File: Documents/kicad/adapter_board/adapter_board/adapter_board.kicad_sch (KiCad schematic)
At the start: 4 parts, among them J1 NPTC081KFXC-RC, J2 NPPN101BFLC-RC, J3 NPPN101BFLC-RC, J4 NPTC081KFXC-RC

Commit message: adapter board changes
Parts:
- J1: value NPTC081KFXC-RC -> ESP Cam Left
- J2: value NPPN101BFLC-RC -> Crazyflie Left
- J3: value NPPN101BFLC-RC -> Crazyflie Right
- J4: value NPTC081KFXC-RC -> ESP Cam Right
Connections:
- net VCOM: now reaches J3.9
- net GND: now reaches J1.7
- net GND: now also J2.10
- net 3.3 V Connect renamed 3v3
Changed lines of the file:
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@@
 	(generator_version "8.0")
 	(paper "A4")
+	(wire
+		(pts
+			(xy 64.77 127) (xy 72.39 127)
+		)
+		(stroke
+			(width 0)
+			(type default)
+		)
+	)
+	(wire
+		(pts
+			(xy 17.78 128.27) (xy 22.86 128.27)
+		)
+		(stroke
+			(width 0)
+			(type default)
+		)
+	)
 	(bus
 		(pts
@@
 		)
 	)
+	(wire
+		(pts
+			(xy 22.86 50.8) (xy 26.67 50.8)
+		)
+		(stroke
+			(width 0)
+			(type default)
+		)
+	)
 	(text "Voltage Step Down"
 		(exclude_from_sim no)
@@
 		)
 	)
-	(label "3.3 V Connect"
+	(label "VCOM"
+		(at 64.77 127 0)
+		(fields_autoplaced yes)
+		(effects
+			(font
+				(size 1.27 1.27)
+			)
+			(justify left bottom)
+		)
+	)
+	(label "GND"
+		(at 17.78 128.27 0)
+		(fields_autoplaced yes)
+		(effects
+			(font
+				(size 1.27 1.27)
+			)
+			(justify left bottom)
+		)
+	)
+	(label "3v3"
 		(at 59.69 54.61 0)
+		(fields_autoplaced yes)
+		(effects
+			(font
+				(size 1.27 1.27)
+			)
+			(justify left bottom)
+		)
+	)
+	(label "GND"
+		(at 22.86 50.8 0)
 		(fields_autoplaced yes)
 		(effects
@@
 			)
 		)
-		(property "Value" "NPPN101BFLC-RC"
+		(property "Value" "Crazyflie Right"
 			(at 86.36 119.3799 0)
 			(effects
@@
 			)
 		)
-		(property "Value" "NPTC081KFXC-RC"
+		(property "Value" "ESP Cam Left"
 			(at 40.64 45.7199 0)
 			(effects
@@
 			)
 		)
-		(property "Value" "NPPN101BFLC-RC"
+		(property "Value" "Crazyflie Left"
 			(at 36.83 118.1099 0)
 			(effects
@@
 			)
 		)
-		(property "Value" "NPTC081KFXC-RC"
+		(property "Value" "ESP Cam Right"
 			(at 86.36 46.9899 0)
 			(effects

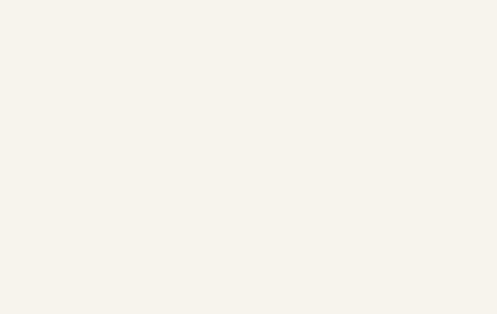
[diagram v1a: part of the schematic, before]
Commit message: adding LEd footprint
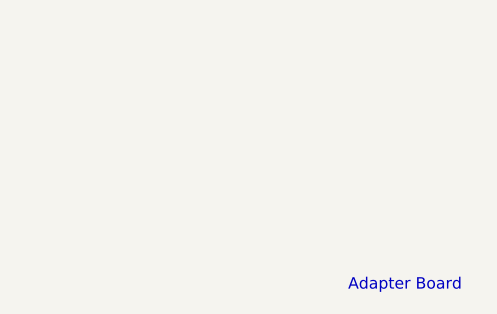
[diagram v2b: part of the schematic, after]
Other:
- note added: "Adapter Board"
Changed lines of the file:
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@@
+		)
+	)
+	(text "Adapter Board"
+		(exclude_from_sim no)
+		(at 195.58 189.484 0)
+		(effects
+			(font
+				(size 1.27 1.27)
+			)
 		)
 	)

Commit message: schematic finished
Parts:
- added C1, C2, C3: 10u, Capacitor_SMD:C_0805_2012Metric_Pad1.18x1.45mm_HandSolder, symbol Device:C
- added C4, C5: 33u, Capacitor_SMD:C_0805_2012Metric_Pad1.18x1.45mm_HandSolder, symbol Device:C
- added JP1: Jumper, Jumper:SolderJumper-2_P1.3mm_Open_TrianglePad1.0x1.5mm, symbol Jumper:SolderJumper_2_Open
- added TP1: Vout LDO, TestPoint:TestPoint_THTPad_1.5x1.5mm_Drill0.7mm, symbol Connector:TestPoint
- added U1: AP2112K-3.3TRG1, footprints:SOT95P285X140-5N, symbol 2024-03-31_17-58-10:AP2112K-3.3TRG1
- J1, J4: footprint CONN_NPTC081KFXC-RC_SUL -> footprints_espcam_connector:CONN_NPTC081KFXC-RC_SUL
- J2, J3: footprint CONN10X1_NPPN101BFLC-RC_SUL -> footprints_crazyflie_connector:CONN10X1_NPPN101BFLC-RC_SUL
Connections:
- net 3v3: now also JP1.2 (B)
- net GND: now also C1.2, C2.2, C3.2, C4.2, C5.2, U1.2 (GND)
- new net: C4.1, C5.1, JP1.1 (A), TP1.1, U1.5 (VOUT)
- new net LDO_IN: C1.1, C2.1, C3.1, U1.1 (VIN), U1.3 (EN)

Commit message: finished board
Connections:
- net VCOM is gone; now on net LDO_IN: J3.9
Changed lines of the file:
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@@
 		)
 	)
-	(label "Vcom"
+	(label "VCOM"
 		(at 129.54 43.18 0)
 		(fields_autoplaced yes)
